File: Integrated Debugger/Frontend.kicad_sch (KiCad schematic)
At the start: 6 parts, among them Q1 NMOS DMN2991UDA-7B, Q2 PMOS DMP32D9UDA-7B, U4 TXB0106RGY

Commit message: feat: finish routing of components
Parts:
- removed Q2: PMOS DMP32D9UDA-7B, Picoballoon ICs:X2-DFN0806-6, symbol Picoballoon ICs:PMOS DMP32D9UDA-7B
- removed R17: 10kΩ, Picoballoon Passives:Resistor 0201, symbol Picoballoon Passives:Resistor
- removed R18: 100Ω, Picoballoon Passives:Resistor 0201, symbol Picoballoon Passives:Resistor
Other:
- note removed: "SUPPLY TARGET POWER SWITCH"
- moved on the sheet: Q1, R16, U4

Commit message: feat: add manufacturing data
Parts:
- Q1: JLCPCB Part # (none) -> C2937136; LCSC Part # (none) -> C2937136; MPN (none) -> DMN2991UDA-7B
- R16: JLCPCB Part # (none) -> C717002; LCSC Part # (none) -> C717002; MPN (none) -> ERJ1GNF1002C
- U4: footprint Package_DFN_QFN:Texas_RGY_R-PVQFN-N16_EP2.05x2.55mm -> Picoballoon ICs:Texas_RGY_R-PVQFN-N16_EP2.05x2.55mm; JLCPCB Part # (none) -> C2652978; LCSC Part # (none) -> C2652978; MPN (none) -> TXB0106RGY
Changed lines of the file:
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@@
 			)
 		)
-		(property "MPN" ""
+		(property "MPN" "ERJ1GNF1002C "
+			(at 69.215 46.355 0)
+			(effects
+				(font
+					(size 1.27 1.27)
+				)
+				(hide yes)
+			)
+		)
+		(property "JLCPCB Part #" "C717002"
+			(at 69.215 46.355 0)
+			(effects
+				(font
+					(size 1.27 1.27)
+				)
+				(hide yes)
+			)
+		)
+		(property "LCSC Part #" "C717002"
 			(at 69.215 46.355 0)
 			(effects
@@
 			)
 		)
-		(property "Footprint" "Package_DFN_QFN:Texas_RGY_R-PVQFN-N16_EP2.05x2.55mm"
+		(property "Footprint" "Picoballoon ICs:Texas_RGY_R-PVQFN-N16_EP2.05x2.55mm"
 			(at 157.48 80.01 0)
 			(effects
@@
 		)
 		(property "Description" "6-Bit Bidirectional Voltage-Level Translator, Auto Direction Sensing and ±15-kV ESD Protection, 1.2 - 3.6V APort, 1.65 - 5.5V BPort, VQFN-16"
+			(at 157.48 60.96 0)
+			(effects
+				(font
+					(size 1.27 1.27)
+				)
+				(hide yes)
+			)
+		)
+		(property "JLCPCB Part #" "C2652978"
+			(at 157.48 60.96 0)
+			(effects
+				(font
+					(size 1.27 1.27)
+				)
+				(hide yes)
+			)
+		)
+		(property "LCSC Part #" "C2652978"
+			(at 157.48 60.96 0)
+			(effects
+				(font
+					(size 1.27 1.27)
+				)
+				(hide yes)
+			)
+		)
+		(property "MPN" "TXB0106RGY"
 			(at 157.48 60.96 0)
 			(effects
@@
 			(effects
 				(font
+					(size 1.27 1.27)
+				)
+				(hide yes)
+			)
+		)
+		(property "JLCPCB Part #" "C2937136 "
+			(at 56.515 65.405 90)
+			(effects
+				(font
+					(size 1.27 1.27)
+				)
+				(hide yes)
+			)
+		)
+		(property "LCSC Part #" "C2937136 "
+			(at 56.515 65.405 90)
+			(effects
+				(font
+					(size 1.27 1.27)
+				)
+				(hide yes)
+			)
+		)
+		(property "MPN" "DMN2991UDA-7B"
+			(at 56.515 65.405 90)
+			(effects
+				(font

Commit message: Revise schematic, add worksheet libraries
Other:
- title: Frontend -> Target frontend
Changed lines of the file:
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@@
 	(paper "A5")
 	(title_block
-		(title "Frontend")
+		(title "Target frontend")
 		(date "2025-08-15")
+		(rev "1.0.0")
 	)
 	(rectangle

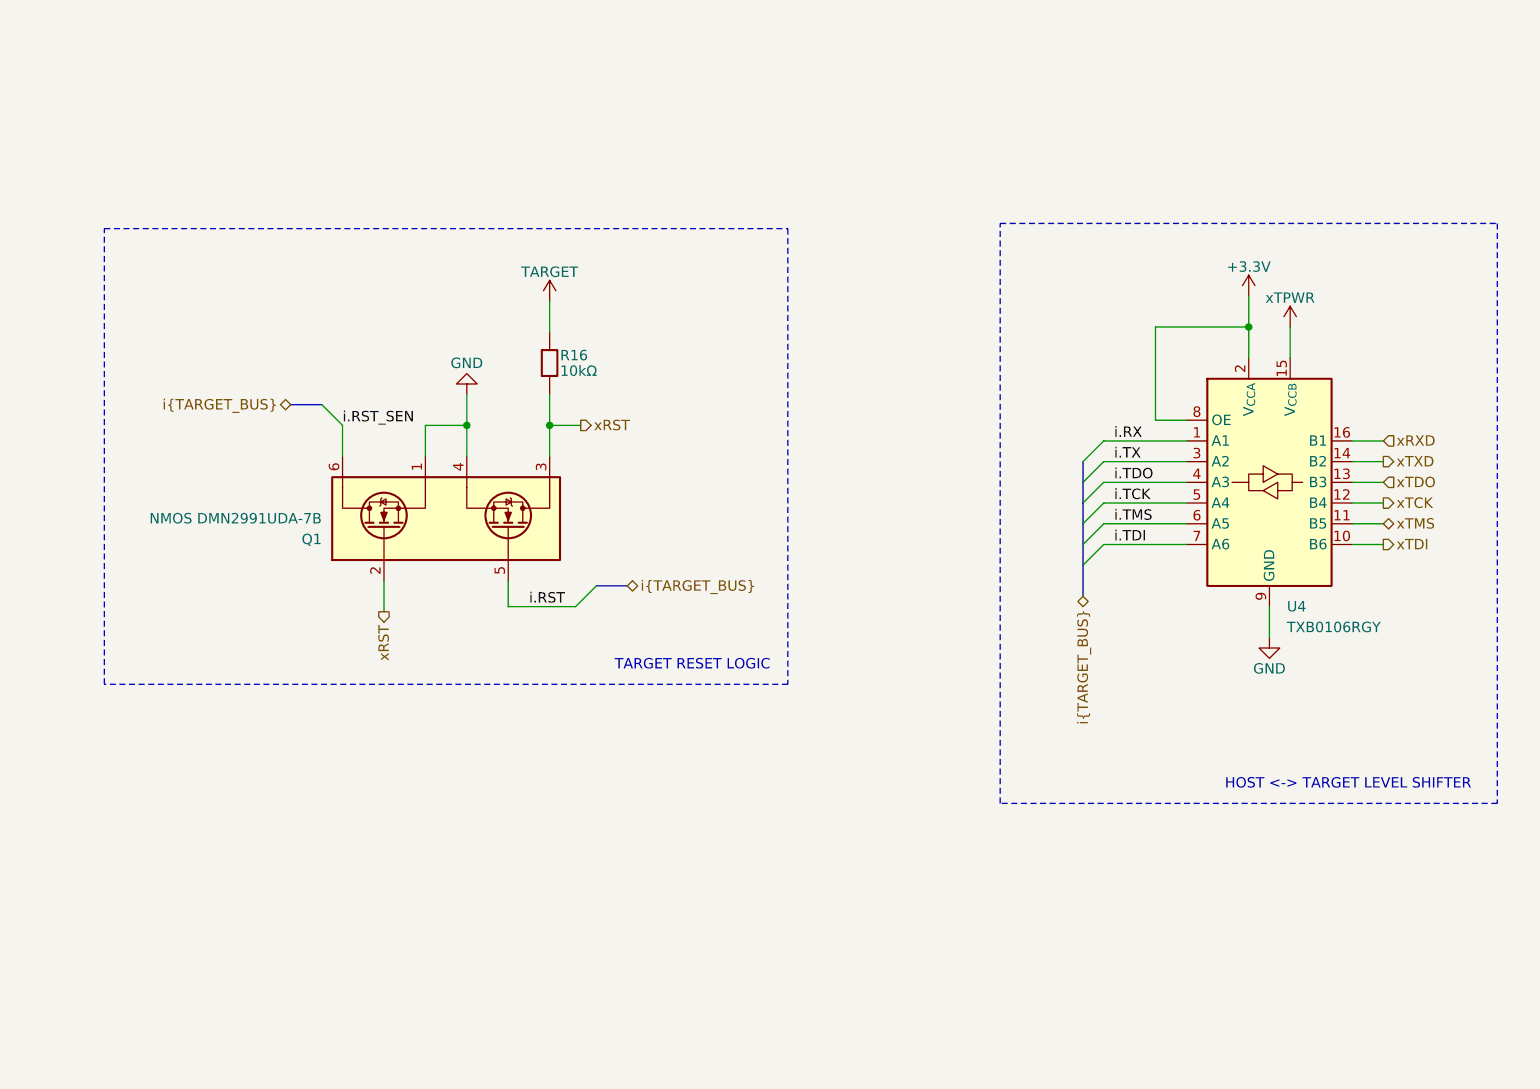
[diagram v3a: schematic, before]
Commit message: Schematic consistency improvements
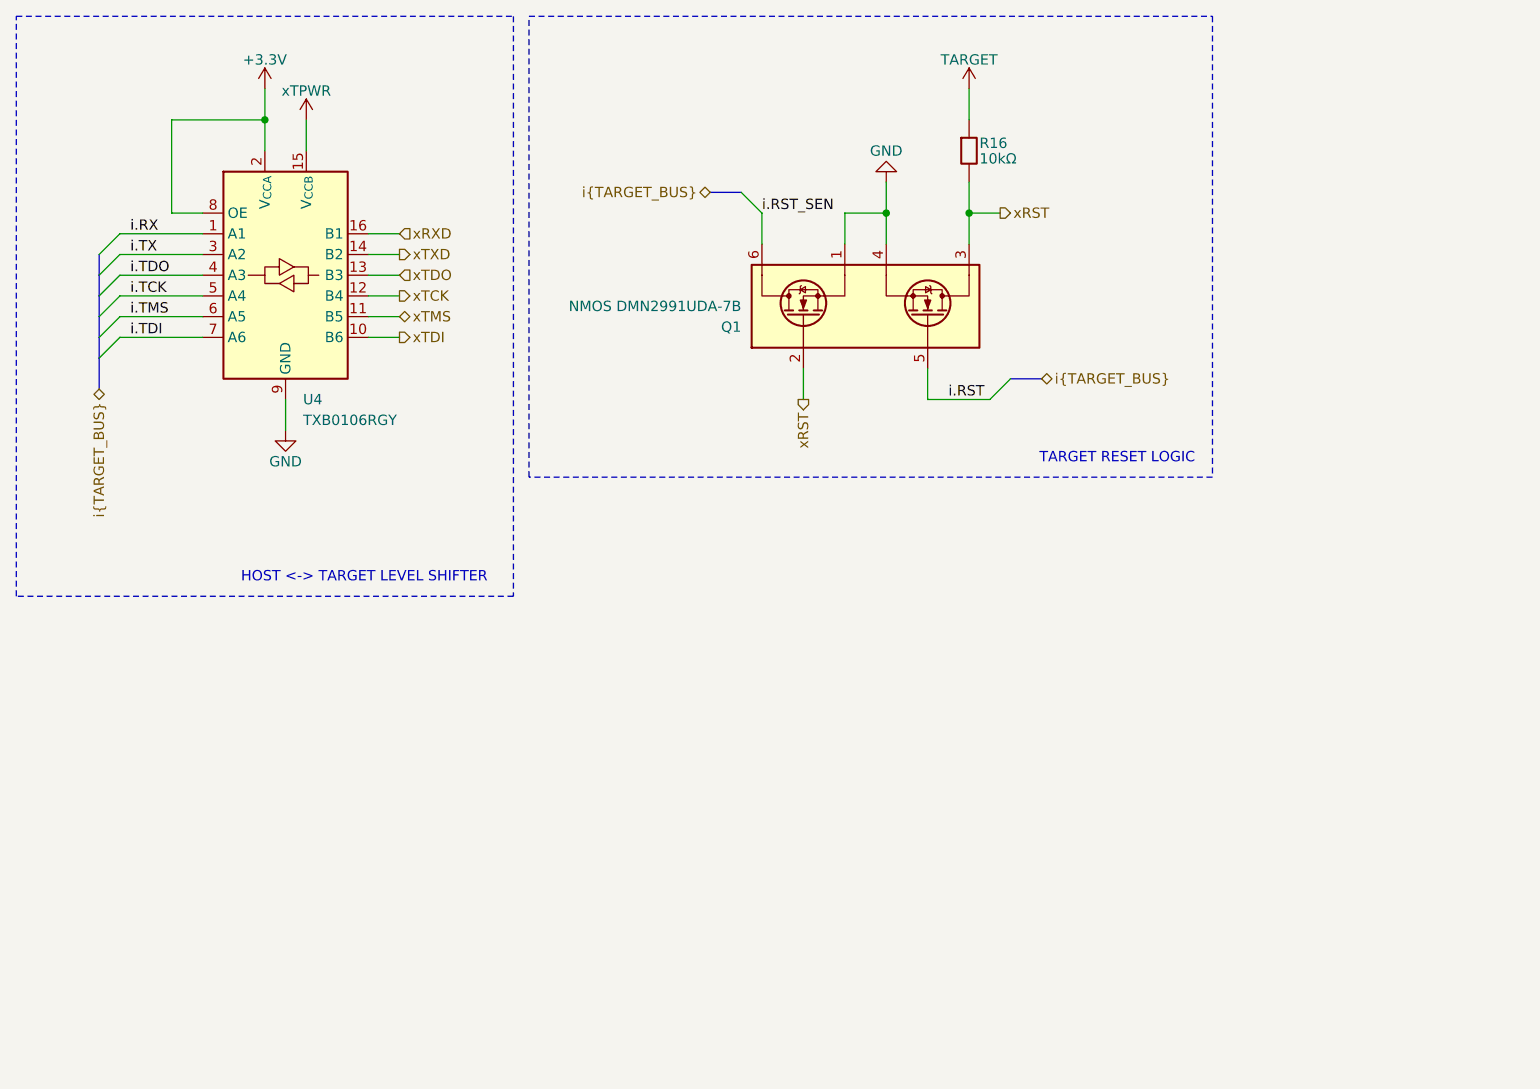
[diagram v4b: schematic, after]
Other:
- moved on the sheet: Q1, R16, U4
